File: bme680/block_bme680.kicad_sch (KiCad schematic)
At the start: 7 parts, among them U1 BME680

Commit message: [Rushil] added default id on skillscreen
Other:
- note added: "Default Address:0x77 when address pin is pulled high"
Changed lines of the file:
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@@
+		)
+	)
+	(text "Default Address:0x77 when address pin is pulled high"
+		(exclude_from_sim no)
+		(at 172.466 121.666 0)
+		(effects
+			(font
+				(size 1.27 1.27)
+			)
 		)
 	)

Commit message: [Rushil] added step file of D1, clean symbol field added default addr
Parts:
- C1, C2, R1, R2: package 0603 -> (none)
- D1: Availability In Stock -> (none); Check_prices https://www.snapeda.com/parts/1N4148WS/Diotec/view-part/?re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 -> (none); Description_1 Small Signal Diode, SOD-323F, 100V, 0.15A, 150°C -> (none); MF Diotec Semiconductor -> (none); MP 1N4148WS -> (none); Package SOD-323F Diotec -> (none); Price None -> (none); SnapEDA_Link https://www.snapeda.com/parts/1N4148WS/Diotec/view-part/?re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 -> (none)
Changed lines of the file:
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@@
-			)
-		)
-		(property "package" "0603"
-			(at 171.45 80.01 0)
-			(effects
-				(font
-					(size 1.27 1.27)
-				)
-				(hide yes)
 			)
 		)
@@
 			)
 		)
-		(property "package" "0603"
-			(at 101.6 82.55 0)
-			(effects
-				(font
-					(size 1.27 1.27)
-				)
-				(hide yes)
-			)
-		)
 		(property "LCSC_part#" "C22399626"
 			(at 101.6 82.55 0)
@@
 					(size 1.27 1.27)
 				)
-				(hide yes)
-			)
-		)
-		(property "MF" "Diotec Semiconductor"
-			(at 187.96 100.33 0)
-			(effects
-				(font
-					(size 1.27 1.27)
-				)
-				(justify bottom)
-				(hide yes)
-			)
-		)
-		(property "Description_1" "Small Signal Diode, SOD-323F, 100V, 0.15A, 150°C"
-			(at 187.96 100.33 0)
-			(effects
-				(font
-					(size 1.27 1.27)
-				)
-				(justify bottom)
-				(hide yes)
-			)
-		)
-		(property "Package" "SOD-323F Diotec"
-			(at 187.96 100.33 0)
-			(effects
-				(font
-					(size 1.27 1.27)
-				)
-				(justify bottom)
-				(hide yes)
-			)
-		)
-		(property "Price" "None"
-			(at 187.96 100.33 0)
-			(effects
-				(font
-					(size 1.27 1.27)
-				)
-				(justify bottom)
-				(hide yes)
-			)
-		)
-		(property "SnapEDA_Link" "https://www.snapeda.com/parts/1N4148WS/Diotec/view-part/?ref=snap"
-			(at 187.96 100.33 0)
-			(effects
-				(font
-					(size 1.27 1.27)
-				)
-				(justify bottom)
-				(hide yes)
-			)
-		)
-		(property "MP" "1N4148WS"
-			(at 187.96 100.33 0)
-			(effects
-				(font
-					(size 1.27 1.27)
-				)
-				(justify bottom)
-				(hide yes)
-			)
-		)
-		(property "Availability" "In Stock"
-			(at 187.96 100.33 0)
-			(effects
-				(font
-					(size 1.27 1.27)
-				)
-				(justify bottom)
-				(hide yes)
-			)
-		)
-		(property "Check_prices" "https://www.snapeda.com/parts/1N4148WS/Diotec/view-part/?ref=eda"
-			(at 187.96 100.33 0)
-			(effects
-				(font
-					(size 1.27 1.27)
-				)
-				(justify bottom)
 				(hide yes)
 			)
@@
 			)
 		)
-		(property "package" "0603"
-			(at 184.15 93.98 0)
-			(effects
-				(font
-					(size 1.27 1.27)
-				)
-				(hide yes)
-			)
-		)
 		(property "LCSC_part#" "C25804"
 			(at 184.15 93.98 0)
@@
 			(at 113.03 82.55 0)
 			(effects
-				(font
-					(size 1.27 1.27)
-				)
-				(hide yes)
-			)
-		)
-		(property "package" "0603"
-			(at 113.03 82.55 0)
-			(effects

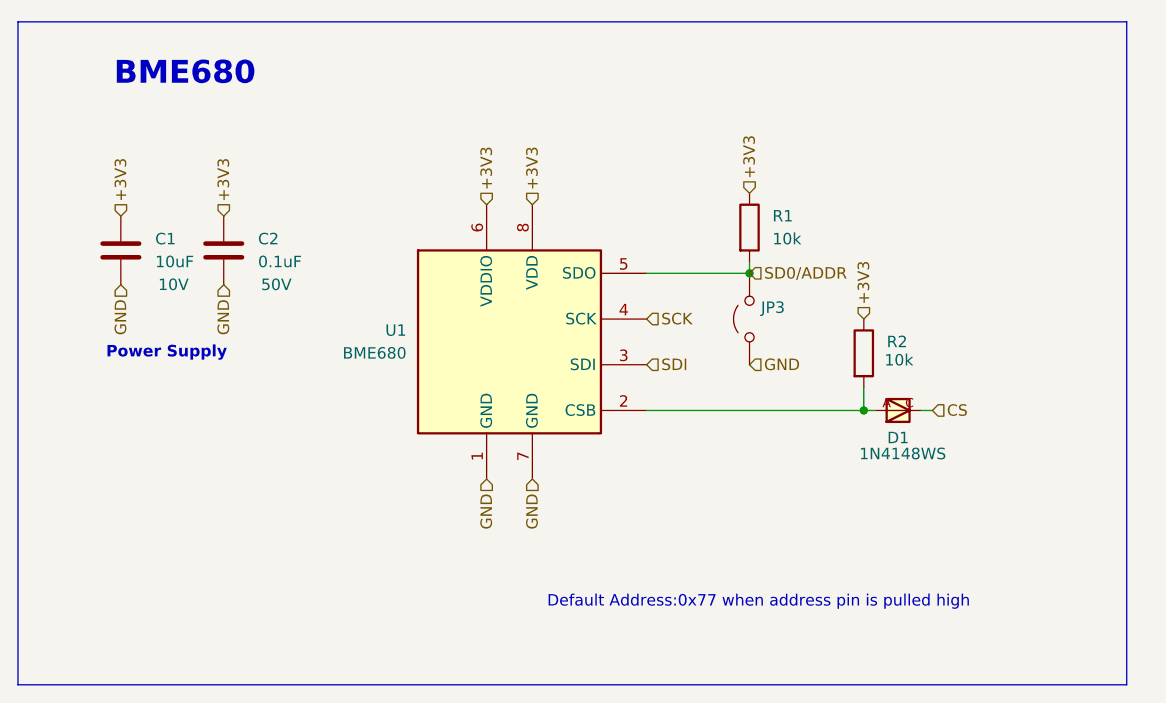
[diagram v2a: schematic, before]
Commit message: [Rushil] corrected pcb added information on both schematic and pcb user drawing correct circuit of bno055
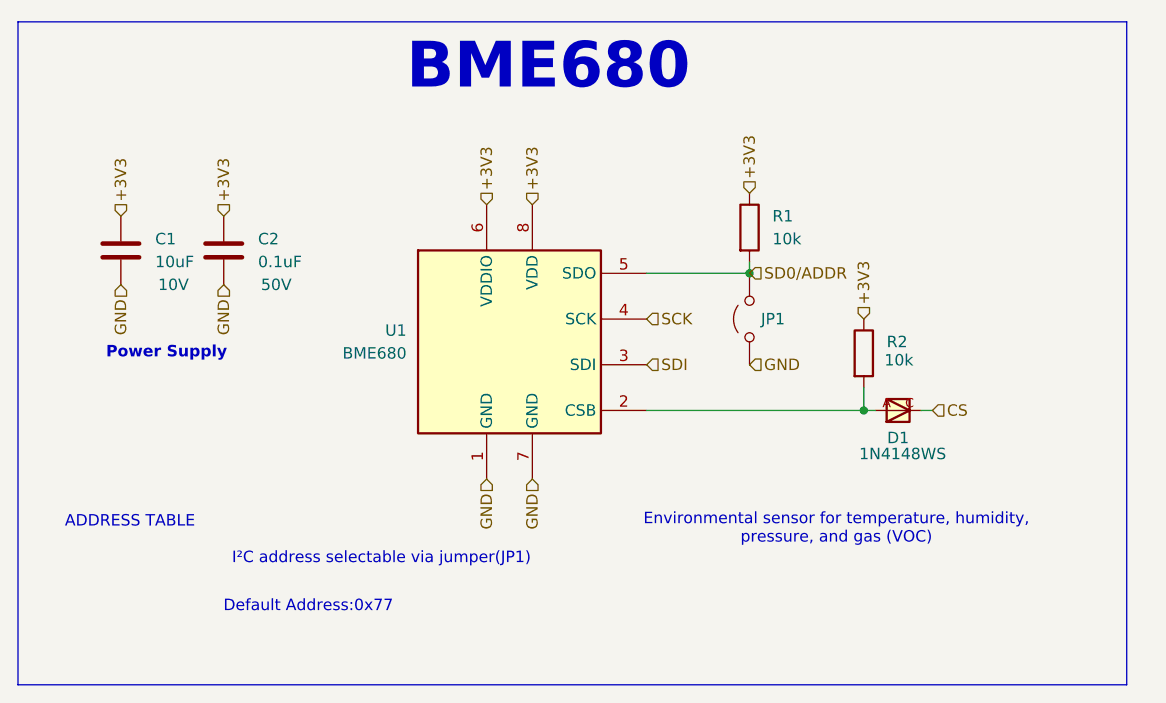
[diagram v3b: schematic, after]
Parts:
- renumbered JP3 to JP1
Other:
- note added: "ADDRESS TABLE"
- note added: "Default Address:0x77"
- note added: "Environmental sensor for temperature, humidity, pressure, and gas (VOC)"
- note added: "I²C address selectable via jumper(JP1)"
- note removed: "Default Address:0x77 when address pin is pulled high"
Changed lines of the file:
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@@
 		)
 	)
-	(text "Default Address:0x77 when address pin is pulled high"
-		(exclude_from_sim no)
-		(at 172.466 121.666 0)
+	(text "Default Address:0x77\n"
+		(exclude_from_sim no)
+		(at 122.428 122.174 0)
+		(effects
+			(font
+				(size 1.27 1.27)
+			)
+		)
+	)
+	(text "ADDRESS TABLE\n"
+		(exclude_from_sim no)
+		(at 102.616 112.776 0)
+		(effects
+			(font
+				(size 1.27 1.27)
+			)
+		)
+	)
+	(text "Environmental sensor for temperature, humidity,\npressure, and gas (VOC)"
+		(exclude_from_sim no)
+		(at 181.102 113.538 0)
+		(effects
+			(font
+				(size 1.27 1.27)
+			)
+		)
+	)
+	(text "I²C address selectable via jumper(JP1)"
+		(exclude_from_sim no)
+		(at 130.556 116.84 0)
 		(effects
 			(font
@@
 	(text "BME680\n"
 		(exclude_from_sim no)
-		(at 108.712 62.992 0)
-		(effects
-			(font
-				(size 2.54 2.54)
-				(thickness 0.508)
+		(at 149.098 62.23 0)
+		(effects
+			(font
+				(size 5.08 5.08)
+				(thickness 1.016)
 				(bold yes)
 			)
@@
 			(width 0)
 			(type default)
+		)
+	)
+	(table
+		(column_count 1)
+		(border
+			(external yes)
+			(header yes)
+			(stroke
+				(width 0)
+				(type solid)
+			)
+		)
+		(separators
+			(rows yes)
+			(cols yes)
+			(stroke
+				(width 0)
+				(type solid)
+			)
+		)
+		(column_widths 6.35)
+		(row_heights 2.54 2.54 2.54)
+		(cells
+			(table_cell "SD0"
+				(exclude_from_sim no)
+				(at 96.52 115.57 0)
+				(size 6.35 2.54)
+				(margins 0.9525 0.9525 0.9525 0.9525)
+				(span 1 1)
+				(fill
+					(type none)
+				)
+				(effects
+					(font
+						(size 1.27 1.27)
+					)
+					(justify left top)
+				)
+			)
+			(table_cell "HIGH"
+				(exclude_from_sim no)
+				(at 96.52 118.11 0)
+				(size 6.35 2.54)
+				(margins 0.9525 0.9525 0.9525 0.9525)
+				(span 1 1)
+				(fill
+					(type none)
+				)
+				(effects
+					(font
+						(size 1.27 1.27)
+					)
+					(justify left top)
+				)
+			)
+			(table_cell "LOW"
+				(exclude_from_sim no)
+				(at 96.52 120.65 0)
+				(size 6.35 2.54)
+				(margins 0.9525 0.9525 0.9525 0.9525)
+				(span 1 1)
+				(fill
+					(type none)
+				)
+				(effects
+					(font
+						(size 1.27 1.27)
+					)
+					(justify left top)
+				)
+			)
+		)
+	)
+	(table
+		(column_count 1)
+		(border
+			(external yes)
+			(header yes)
+			(stroke
+				(width 0)
+				(type solid)
+			)
+		)
+		(separators
+			(rows yes)
+			(cols yes)
+			(stroke
+				(width 0)
+				(type solid)
+			)
+		)
+		(column_widths 7.62)
+		(row_heights 2.54 2.54 2.54)
+		(cells
+			(table_cell "ADDR"
+				(exclude_from_sim no)
+				(at 102.87 115.57 0)
+				(size 7.62 2.54)
+				(margins 0.9525 0.9525 0.9525 0.9525)
+				(span 1 1)
+				(fill
+					(type none)
+				)
+				(effects
+					(font
+						(size 1.27 1.27)
+					)
+					(justify left top)
+				)
+			)
+			(table_cell "0X76"
+				(exclude_from_sim no)
+				(at 102.87 118.11 0)
+				(size 7.62 2.54)
+				(margins 0.9525 0.9525 0.9525 0.9525)
+				(span 1 1)
+				(fill
+					(type none)
+				)
+				(effects
+					(font
+						(size 1.27 1.27)
+					)
+					(justify left top)
+				)
+			)
+			(table_cell "0X77"
+				(exclude_from_sim no)
+				(at 102.87 120.65 0)
+				(size 7.62 2.54)
+				(margins 0.9525 0.9525 0.9525 0.9525)
+				(span 1 1)
+				(fill
+					(type none)
+				)
+				(effects
+					(font
+						(size 1.27 1.27)
+					)
+					(justify left top)
+				)
+			)
 		)
 	)
@@
 		(dnp no)
 		(fields_autoplaced yes)
-		(property "Reference" "JP3"
-			(at 172.72 88.8999 90)
+		(property "Reference" "JP1"
+			(at 172.72 90.1699 90)
 			(effects
 				(font
@@
 			(project "bme680"
 				(path "/419bc571-068d-4021-a70d-c9d5ede62e1d/0b452597-2969-4c44-9bd0-751bfc0daaa3"
-					(reference "JP3")
+					(reference "JP1")
 					(unit 1)
 				)

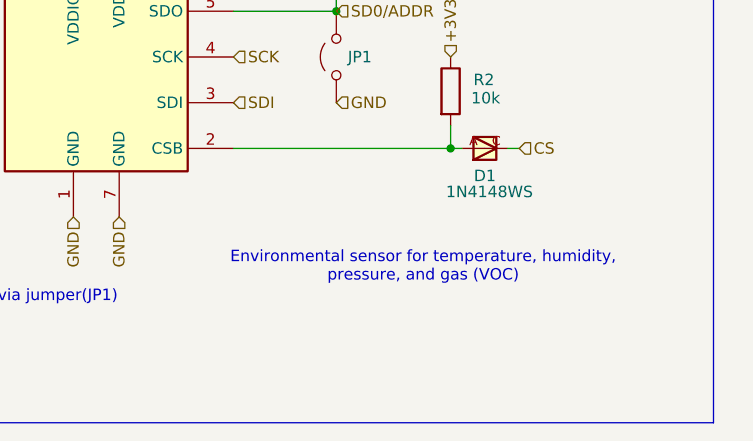
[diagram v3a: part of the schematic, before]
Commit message: [Rushil] added ams1117-3.3 block and did some clean up in schematic info part
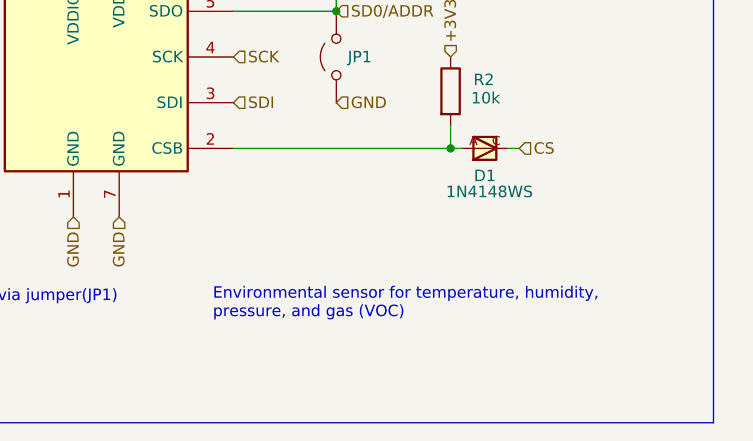
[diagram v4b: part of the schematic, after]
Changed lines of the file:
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@@
 	(text "Environmental sensor for temperature, humidity,\npressure, and gas (VOC)"
 		(exclude_from_sim no)
-		(at 181.102 113.538 0)
+		(at 157.734 117.602 0)
 		(effects
 			(font
 				(size 1.27 1.27)
 			)
+			(justify left)
 		)
 	)

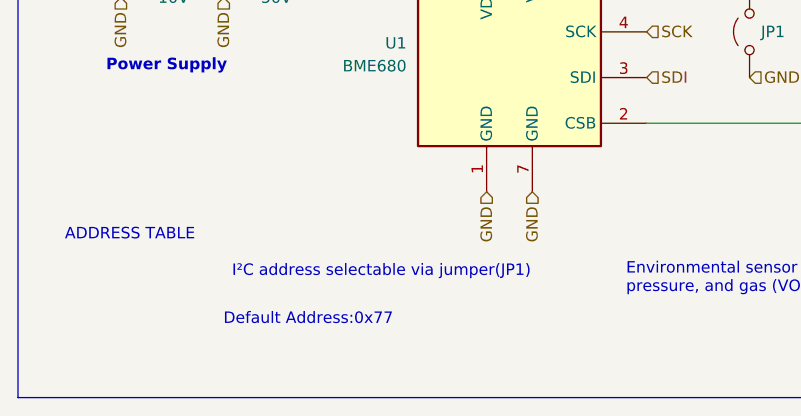
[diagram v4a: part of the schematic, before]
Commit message: bug fixes in BME680
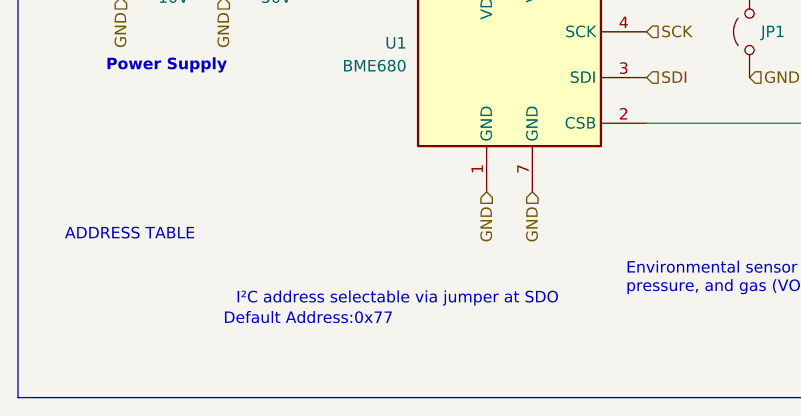
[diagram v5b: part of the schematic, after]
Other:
- note added: "I²C address selectable via jumper at SDO"
- note removed: "I²C address selectable via jumper(JP1)"
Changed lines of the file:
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@@
 		)
 	)
-	(text "I²C address selectable via jumper(JP1)"
+	(text "I²C address selectable via jumper at SDO"
 		(exclude_from_sim no)
-		(at 130.556 116.84 0)
+		(at 132.334 119.888 0)
 		(effects
 			(font
